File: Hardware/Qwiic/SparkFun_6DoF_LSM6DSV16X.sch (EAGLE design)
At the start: 37 parts, among them J1 QWIIC_RIGHT_ANGLE, J2 QWIIC_RIGHT_ANGLE, U2 LSM6DSV16X

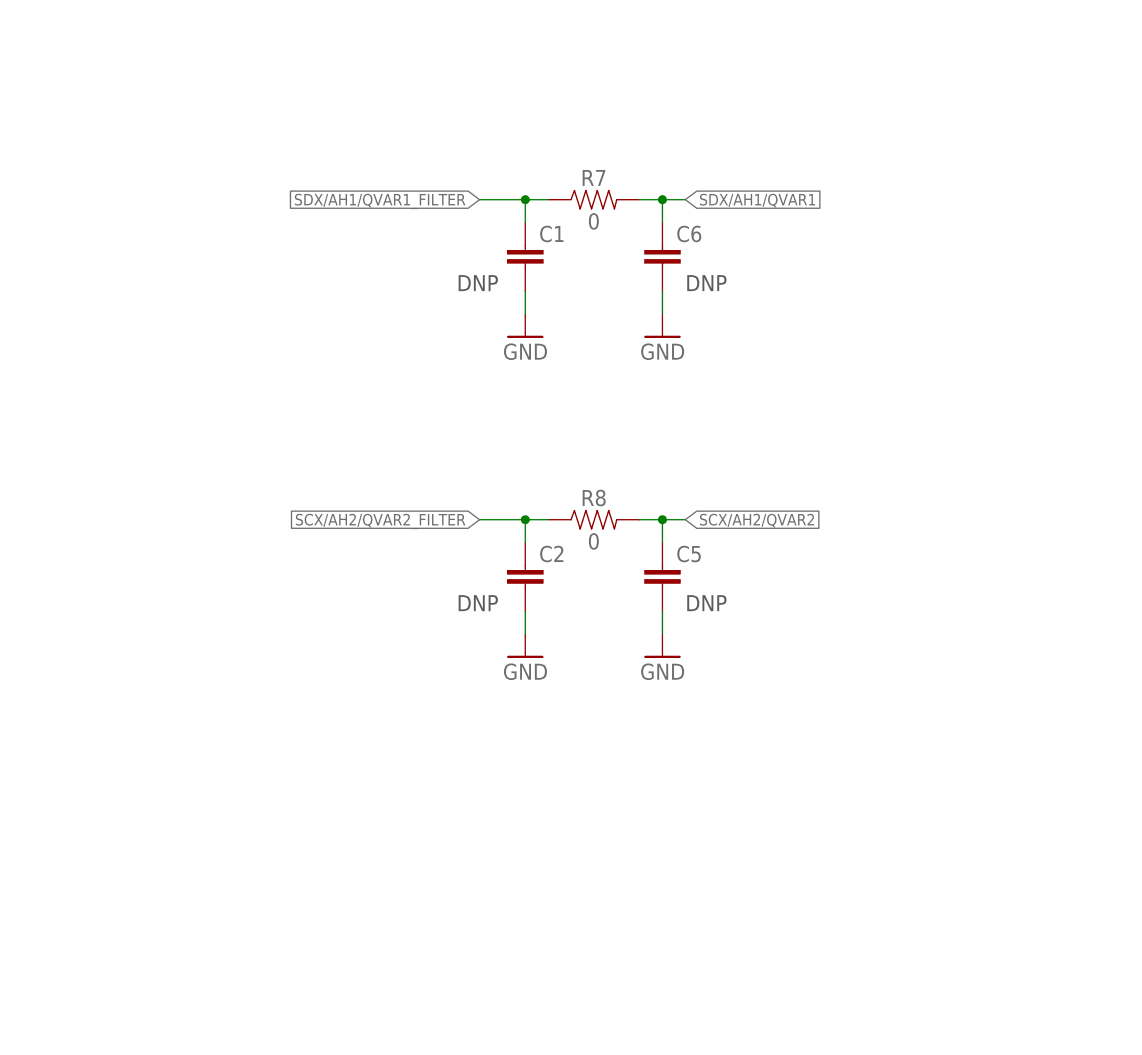
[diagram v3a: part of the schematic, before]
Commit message: Adds note about "Qvar sensing"
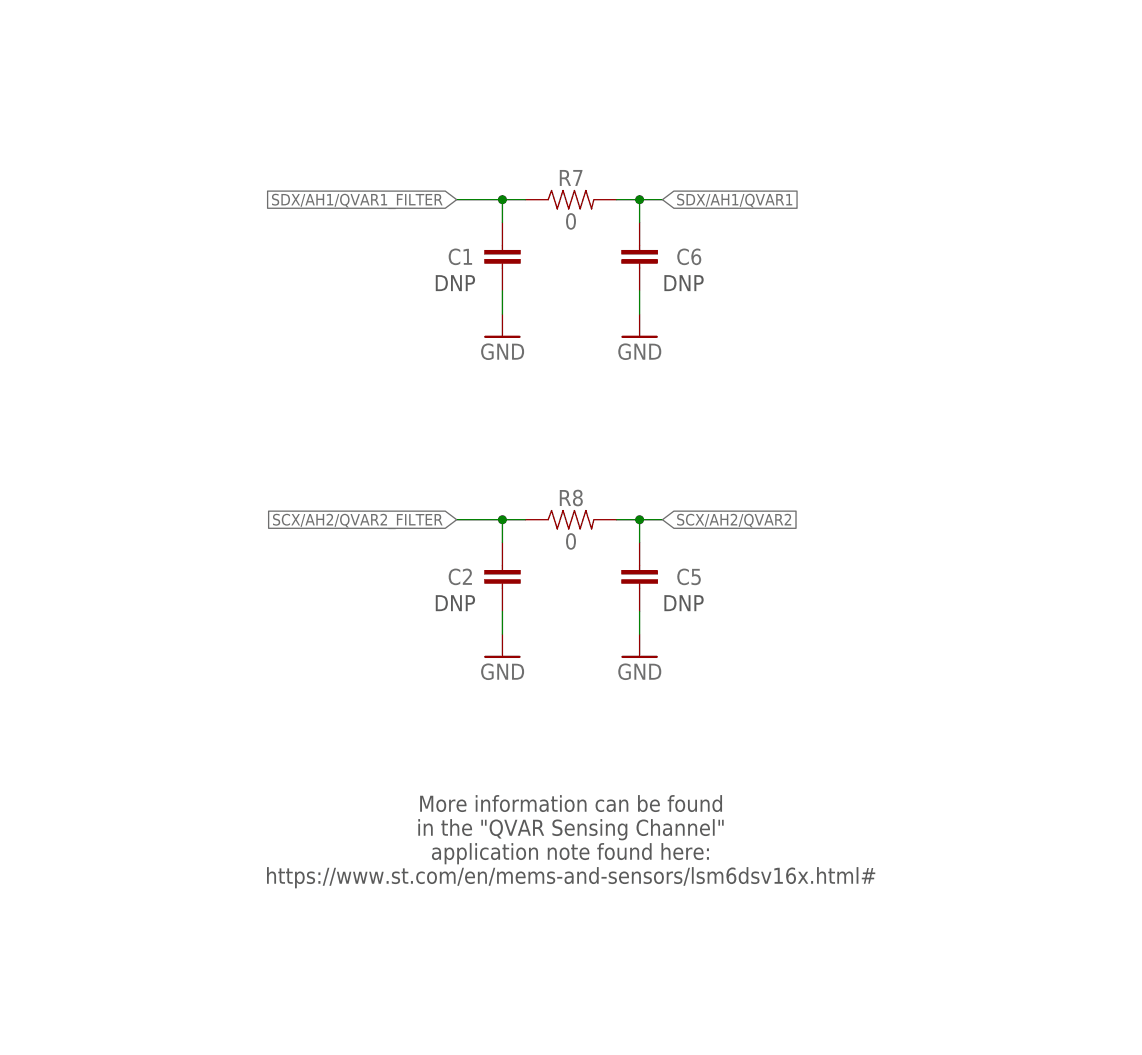
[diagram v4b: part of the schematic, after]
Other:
- note added: "More information can be found in the "QVAR Sensing Channel" application note found here: https://www.st.com/en/mems-and-sensors/lsm6dsv16x.html#"
- moved on the sheet: C1, C2, C5, C6, R7, R8
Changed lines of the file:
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@@
 <text x="76.2" y="124.46" size="1.778" layer="97" font="vector" align="center">Cut SCX and SDX jumpers to utilize analog
 input cabalities (see "Jumpers" section).</text>
-<text x="63.5" y="86.36" size="1.778" layer="97" font="vector">DNP</text>
-<text x="88.9" y="86.36" size="1.778" layer="97" font="vector">DNP</text>
-<text x="63.5" y="50.8" size="1.778" layer="97" font="vector">DNP</text>
-<text x="88.9" y="50.8" size="1.778" layer="97" font="vector">DNP</text>
+<text x="60.96" y="86.36" size="1.778" layer="97" font="vector">DNP</text>
+<text x="86.36" y="86.36" size="1.778" layer="97" font="vector">DNP</text>
+<text x="60.96" y="50.8" size="1.778" layer="97" font="vector">DNP</text>
+<text x="86.36" y="50.8" size="1.778" layer="97" font="vector">DNP</text>
+<text x="76.2" y="25.4" size="1.778" layer="97" font="vector" align="center">More information can be found
+in the "QVAR Sensing Channel"
+application note found here:
+https://www.st.com/en/mems-and-sensors/lsm6dsv16x.html#
+</text>
 </plain>
 <instances>
@@
 <attribute name="VALUE" x="88.9" y="198.12" size="1.778" layer="96" font="vector" align="center"/>
 </instance>
-<instance part="C1" gate="G$1" x="71.12" y="88.9" smashed="yes">
-<attribute name="NAME" x="72.644" y="91.821" size="1.778" layer="95" font="vector"/>
-</instance>
-<instance part="C2" gate="G$1" x="71.12" y="53.34" smashed="yes">
-<attribute name="NAME" x="72.644" y="56.261" size="1.778" layer="95" font="vector"/>
-</instance>
-<instance part="R7" gate="G$1" x="78.74" y="96.52" smashed="yes">
-<attribute name="NAME" x="78.74" y="98.044" size="1.778" layer="95" font="vector" align="bottom-center"/>
-<attribute name="VALUE" x="78.74" y="94.996" size="1.778" layer="96" font="vector" align="top-center"/>
-</instance>
-<instance part="R8" gate="G$1" x="78.74" y="60.96" smashed="yes">
-<attribute name="NAME" x="78.74" y="62.484" size="1.778" layer="95" font="vector" align="bottom-center"/>
-<attribute name="VALUE" x="78.74" y="59.436" size="1.778" layer="96" font="vector" align="top-center"/>
-</instance>
-<instance part="GND8" gate="1" x="71.12" y="81.28" smashed="yes" rot="MR0">
-<attribute name="VALUE" x="73.66" y="78.74" size="1.778" layer="96" font="vector" rot="MR0"/>
-</instance>
-<instance part="GND9" gate="1" x="86.36" y="81.28" smashed="yes" rot="MR0">
-<attribute name="VALUE" x="88.9" y="78.74" size="1.778" layer="96" font="vector" rot="MR0"/>
-</instance>
-<instance part="GND12" gate="1" x="71.12" y="45.72" smashed="yes" rot="MR0">
-<attribute name="VALUE" x="73.66" y="43.18" size="1.778" layer="96" font="vector" rot="MR0"/>
-</instance>
-<instance part="GND13" gate="1" x="86.36" y="45.72" smashed="yes" rot="MR0">
-<attribute name="VALUE" x="88.9" y="43.18" size="1.778" layer="96" font="vector" rot="MR0"/>
+<instance part="C1" gate="G$1" x="68.58" y="88.9" smashed="yes">
+<attribute name="NAME" x="62.484" y="89.281" size="1.778" layer="95" font="vector"/>
+</instance>
+<instance part="C2" gate="G$1" x="68.58" y="53.34" smashed="yes">
+<attribute name="NAME" x="62.484" y="53.721" size="1.778" layer="95" font="vector"/>
+</instance>
+<instance part="R7" gate="G$1" x="76.2" y="96.52" smashed="yes">
+<attribute name="NAME" x="76.2" y="98.044" size="1.778" layer="95" font="vector" align="bottom-center"/>
+<attribute name="VALUE" x="76.2" y="94.996" size="1.778" layer="96" font="vector" align="top-center"/>
+</instance>
+<instance part="R8" gate="G$1" x="76.2" y="60.96" smashed="yes">
+<attribute name="NAME" x="76.2" y="62.484" size="1.778" layer="95" font="vector" align="bottom-center"/>
+<attribute name="VALUE" x="76.2" y="59.436" size="1.778" layer="96" font="vector" align="top-center"/>
+</instance>
+<instance part="GND8" gate="1" x="68.58" y="81.28" smashed="yes" rot="MR0">
+<attribute name="VALUE" x="71.12" y="78.74" size="1.778" layer="96" font="vector" rot="MR0"/>
+</instance>
+<instance part="GND9" gate="1" x="83.82" y="81.28" smashed="yes" rot="MR0">
+<attribute name="VALUE" x="86.36" y="78.74" size="1.778" layer="96" font="vector" rot="MR0"/>
+</instance>
+<instance part="GND12" gate="1" x="68.58" y="45.72" smashed="yes" rot="MR0">
+<attribute name="VALUE" x="71.12" y="43.18" size="1.778" layer="96" font="vector" rot="MR0"/>
+</instance>
+<instance part="GND13" gate="1" x="83.82" y="45.72" smashed="yes" rot="MR0">
+<attribute name="VALUE" x="86.36" y="43.18" size="1.778" layer="96" font="vector" rot="MR0"/>
 </instance>
 <instance part="FRAME2" gate="G$1" x="0" y="0" smashed="yes"/>
@@
 <attribute name="REV" x="419.1" y="6.604" size="2.7432" layer="94" font="vector"/>
 </instance>
-<instance part="C5" gate="G$1" x="86.36" y="53.34" smashed="yes">
-<attribute name="NAME" x="87.884" y="56.261" size="1.778" layer="95" font="vector"/>
-</instance>
-<instance part="C6" gate="G$1" x="86.36" y="88.9" smashed="yes">
-<attribute name="NAME" x="87.884" y="91.821" size="1.778" layer="95" font="vector"/>
+<instance part="C5" gate="G$1" x="83.82" y="53.34" smashed="yes">
+<attribute name="NAME" x="87.884" y="53.721" size="1.778" layer="95" font="vector"/>
+</instance>
+<instance part="C6" gate="G$1" x="83.82" y="88.9" smashed="yes">
+<attribute name="NAME" x="87.884" y="89.281" size="1.778" layer="95" font="vector"/>
 </instance>
 <instance part="STANDOFF4" gate="G$1" x="426.72" y="30.48" smashed="yes"/>
@@
 <pinref part="C1" gate="G$1" pin="2"/>
 <pinref part="GND8" gate="1" pin="GND"/>
-<wire x1="71.12" y1="83.82" x2="71.12" y2="86.36" width="0.1524" layer="91"/>
+<wire x1="68.58" y1="83.82" x2="68.58" y2="86.36" width="0.1524" layer="91"/>
 </segment>
 <segment>
 <pinref part="GND9" gate="1" pin="GND"/>
-<wire x1="86.36" y1="83.82" x2="86.36" y2="86.36" width="0.1524" layer="91"/>
+<wire x1="83.82" y1="83.82" x2="83.82" y2="86.36" width="0.1524" layer="91"/>
 <pinref part="C6" gate="G$1" pin="2"/>
 </segment>
@@
 <pinref part="C2" gate="G$1" pin="2"/>
 <pinref part="GND12" gate="1" pin="GND"/>
-<wire x1="71.12" y1="48.26" x2="71.12" y2="50.8" width="0.1524" layer="91"/>
+<wire x1="68.58" y1="48.26" x2="68.58" y2="50.8" width="0.1524" layer="91"/>
 </segment>
 <segment>
 <pinref part="GND13" gate="1" pin="GND"/>
-<wire x1="86.36" y1="48.26" x2="86.36" y2="50.8" width="0.1524" layer="91"/>
+<wire x1="83.82" y1="48.26" x2="83.82" y2="50.8" width="0.1524" layer="91"/>
 <pinref part="C5" gate="G$1" pin="2"/>
 </segment>
@@
 <pinref part="R7" gate="G$1" pin="1"/>
 <pinref part="C1" gate="G$1" pin="1"/>
-<wire x1="71.12" y1="96.52" x2="73.66" y2="96.52" width="0.1524" layer="91"/>
-<wire x1="71.12" y1="93.98" x2="71.12" y2="96.52" width="0.1524" layer="91"/>
-<junction x="71.12" y="96.52"/>
-<label x="66.04" y="96.52" size="1.27" layer="95" font="vector" rot="R180" xref="yes"/>
-<wire x1="71.12" y1="96.52" x2="66.04" y2="96.52" width="0.1524" layer="91"/>
+<wire x1="68.58" y1="96.52" x2="71.12" y2="96.52" width="0.1524" layer="91"/>
+<wire x1="68.58" y1="93.98" x2="68.58" y2="96.52" width="0.1524" layer="91"/>
+<junction x="68.58" y="96.52"/>
+<label x="63.5" y="96.52" size="1.27" layer="95" font="vector" rot="R180" xref="yes"/>
+<wire x1="68.58" y1="96.52" x2="63.5" y2="96.52" width="0.1524" layer="91"/>
 </segment>
 </net>
@@
 <segment>
 <pinref part="R8" gate="G$1" pin="1"/>
-<wire x1="73.66" y1="60.96" x2="71.12" y2="60.96" width="0.1524" layer="91"/>
+<wire x1="71.12" y1="60.96" x2="68.58" y2="60.96" width="0.1524" layer="91"/>
 <pinref part="C2" gate="G$1" pin="1"/>
-<wire x1="71.12" y1="58.42" x2="71.12" y2="60.96" width="0.1524" layer="91"/>
-<junction x="71.12" y="60.96"/>
-<label x="66.04" y="60.96" size="1.27" layer="95" font="vector" rot="R180" xref="yes"/>
-<wire x1="71.12" y1="60.96" x2="66.04" y2="60.96" width="0.1524" layer="91"/>
+<wire x1="68.58" y1="58.42" x2="68.58" y2="60.96" width="0.1524" layer="91"/>
+<junction x="68.58" y="60.96"/>
+<label x="63.5" y="60.96" size="1.27" layer="95" font="vector" rot="R180" xref="yes"/>
+<wire x1="68.58" y1="60.96" x2="63.5" y2="60.96" width="0.1524" layer="91"/>
 </segment>
 </net>
@@
 <segment>
 <pinref part="R7" gate="G$1" pin="2"/>
+<wire x1="81.28" y1="96.52" x2="83.82" y2="96.52" width="0.1524" layer="91"/>
 <wire x1="83.82" y1="96.52" x2="86.36" y2="96.52" width="0.1524" layer="91"/>
-<wire x1="86.36" y1="96.52" x2="88.9" y2="96.52" width="0.1524" layer="91"/>
-<wire x1="86.36" y1="93.98" x2="86.36" y2="96.52" width="0.1524" layer="91"/>
-<junction x="86.36" y="96.52"/>
-<label x="88.9" y="96.52" size="1.27" layer="95" font="vector" xref="yes"/>
+<wire x1="83.82" y1="93.98" x2="83.82" y2="96.52" width="0.1524" layer="91"/>
+<junction x="83.82" y="96.52"/>
+<label x="86.36" y="96.52" size="1.27" layer="95" font="vector" xref="yes"/>
 <pinref part="C6" gate="G$1" pin="1"/>
 </segment>
@@
 <segment>
 <pinref part="R8" gate="G$1" pin="2"/>
+<wire x1="81.28" y1="60.96" x2="83.82" y2="60.96" width="0.1524" layer="91"/>
 <wire x1="83.82" y1="60.96" x2="86.36" y2="60.96" width="0.1524" layer="91"/>
-<wire x1="86.36" y1="60.96" x2="88.9" y2="60.96" width="0.1524" layer="91"/>
-<wire x1="86.36" y1="58.42" x2="86.36" y2="60.96" width="0.1524" layer="91"/>
-<junction x="86.36" y="60.96"/>
-<label x="88.9" y="60.96" size="1.27" layer="95" font="vector" xref="yes"/>
+<wire x1="83.82" y1="58.42" x2="83.82" y2="60.96" width="0.1524" layer="91"/>
+<junction x="83.82" y="60.96"/>
+<label x="86.36" y="60.96" size="1.27" layer="95" font="vector" xref="yes"/>
 <pinref part="C5" gate="G$1" pin="1"/>
 </segment>

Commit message: Adds jumpers for one of the DNP pads to select whether it's tied to 3v3 or GND
* Rolls to v10
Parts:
- removed C1, C2: 110pF, SparkFun-Capacitors:CAP-0603
- removed LOGO3: SFE_LOGO_NAME_FLAME.1_INCH, SparkFun-Aesthetics:SFE_LOGO_NAME_FLAME.1_INCH
- added P1, P2: 110pF, SparkFun-Capacitors:CAP-0603
- added PAD1, PAD2: JUMPER-SMT_3_1-NC_TRACE_SILK, SparkFun-Jumpers:JUMPER-SMT_3_1-NC_TRACE_SILK
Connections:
- new net N$4: P2.2, PAD2.2
- new net N$8: P1.2, PAD1.2
- net 3.3V: now also PAD1.1, PAD2.1
- net GND: now also PAD1.3, PAD2.3; no longer C1.2, C2.2
- net SCX/AH2/QVAR2_FILTER: now also P2.1; no longer C2.1
- net SDX/AH1/QVAR1_FILTER: now also P1.1; no longer C1.1
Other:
- note added: "You can select whether P1 is tied to GND or tied to 3v (1) using the PAD1 jumper."
- note added: "You can select whether P2 is tied to GND or tied to 3v3(1) using the PAD2 jumper."
- moved on the sheet: C5, C6, R7, R8

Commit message: Adds slightly better silk to new three way jumper
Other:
- note added: "You can select whether P1 is tied to GND (0) or tied to 3v3 (1) using the PAD1 jumper."
- note added: "You can select whether P2 is tied to GND (0) or tied to 3v3 (1) using the PAD2 jumper."
- note added: "v10"
- note removed: "You can select whether P1 is tied to GND or tied to 3v (1) using the PAD1 jumper."
- note removed: "You can select whether P2 is tied to GND or tied to 3v3(1) using the PAD2 jumper."
- note removed: "v01"
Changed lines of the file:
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@@
 <text x="93.726" y="261.874" size="1.27" layer="97" font="vector">VDD Range: 1.71V - 3.6V
 VDDIO Range: 1.62V - 3.6V</text>
-<text x="421.64" y="7.62" size="2.54" layer="94" font="vector">v01</text>
+<text x="421.64" y="7.62" size="2.54" layer="94" font="vector">v10</text>
 <text x="325.12" y="271.78" size="2.54" layer="94" font="vector" align="center">Jumpers</text>
 <text x="340.36" y="213.36" size="1.778" layer="97" font="vector">Cut trace to
@@
 https://www.st.com/en/mems-and-sensors/lsm6dsv16x.html#
 </text>
-<text x="68.58" y="76.2" size="1.778" layer="97" font="vector" align="center">You can select whether P1 is tied to GND
-or tied to 3v (1) using the PAD1 jumper.</text>
-<text x="66.04" y="30.48" size="1.778" layer="97" font="vector" align="center">You can select whether P2 is tied to GND
-or tied to 3v3(1) using the PAD2 jumper.</text>
+<text x="68.58" y="76.2" size="1.778" layer="97" font="vector" align="center">You can select whether P1 is tied to
+GND (0) or tied to 3v3 (1) using the PAD1 jumper.</text>
+<text x="66.04" y="30.48" size="1.778" layer="97" font="vector" align="center">You can select whether P2 is tied to
+GND (0) or tied to 3v3 (1) using the PAD2 jumper.</text>
 </plain>
 <instances>

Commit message: Increases pad size, decreases paste size on footprint
* Also adds trestrict between ground pads to the footprint itself
* Fixes gyro silk on bottom
* Swaps PICO and CS on 1x1 header
* Improves ground pour
* Adds more notes to the filter section
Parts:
- added LOGO3: SFE_LOGO_NAME_FLAMEBLANK, SparkFun-Aesthetics:SFE_LOGO_NAME_FLAMEBLANK
- D1: device SparkFun-LED:LED-RED0603 -> SparkFun-LED:LED-RED_0603-KB
- R4: value 1k -> 4.7k; device SparkFun-Resistors:1KOHM-0603-1/10W-1% -> SparkFun-Resistors:4.7KOHM-0603-1/10W-1%
- renumbered U2 to U1
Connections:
- removed net SCL: J1.4, J2.4, JP1.3, R1.1, U1.SCL
- new net SCL/SCLK: J1.4, J2.4, JP1.3, R1.1, U1.SCL/SPC
- net !CS!: now also JP1.1; no longer JP1.2
- net POCI/SA0: now also JP1.2; no longer JP1.1
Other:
- note added: "6DoF IMU - LSM6DSV16X"
- note added: "Analog In (QVar) - Filter Circuit"
- note added: "Some suggested configurations might include a voltage divider or capacitor-resistor-diode. More information can be found in the "QVAR Sensing Channel" application note found here: https://www.st.com/en/mems-and-sensors/lsm6dsv16x.html#"
- note removed: "Accelerometer - LSM6DSV16X"
- note removed: "Filter Circuit - Analog In"
- note removed: "More information can be found in the "QVAR Sensing Channel" application note found here: https://www.st.com/en/mems-and-sensors/lsm6dsv16x.html#"
